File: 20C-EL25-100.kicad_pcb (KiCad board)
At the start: 2 copper layers, 65.5 x 23.5 mm, 9 parts, among them J1 Conn_01x04

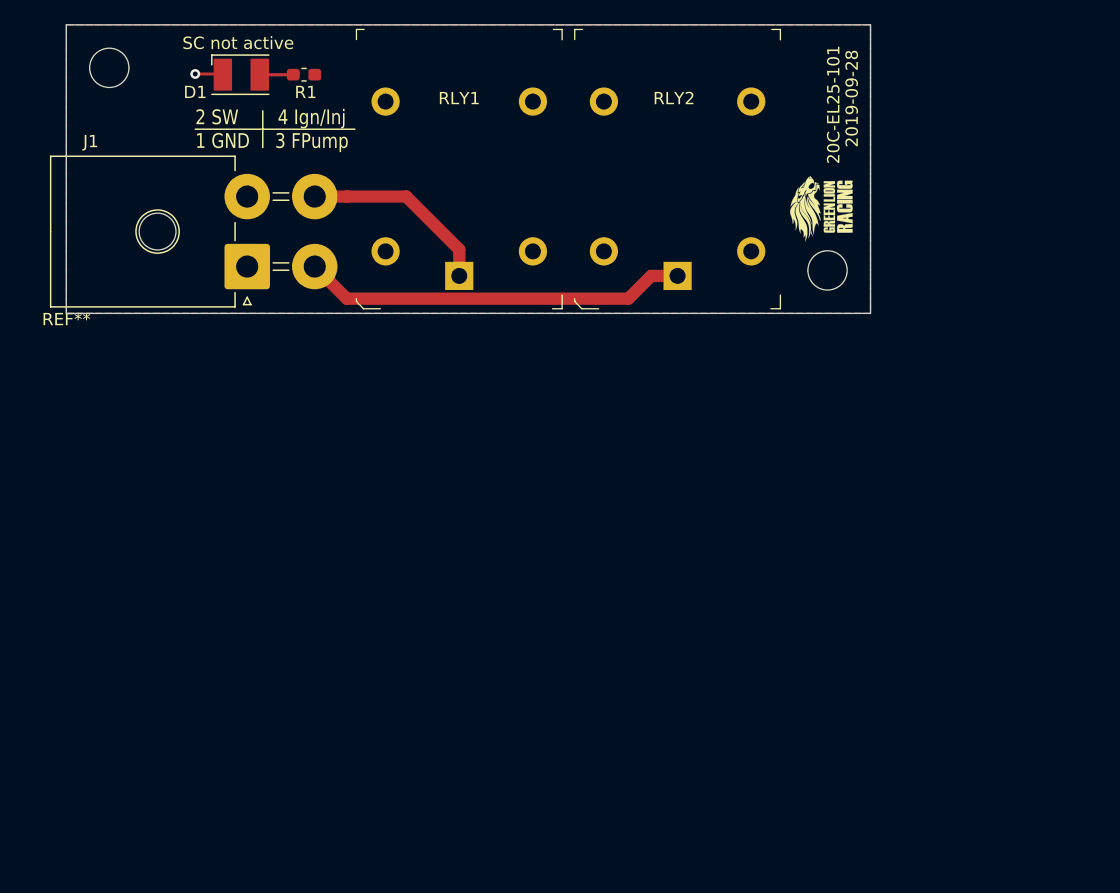
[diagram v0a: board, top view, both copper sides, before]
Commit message: added 3. relays to pcb
added 12V relays on pcb to support our ignition (lowside FET inside MCU)
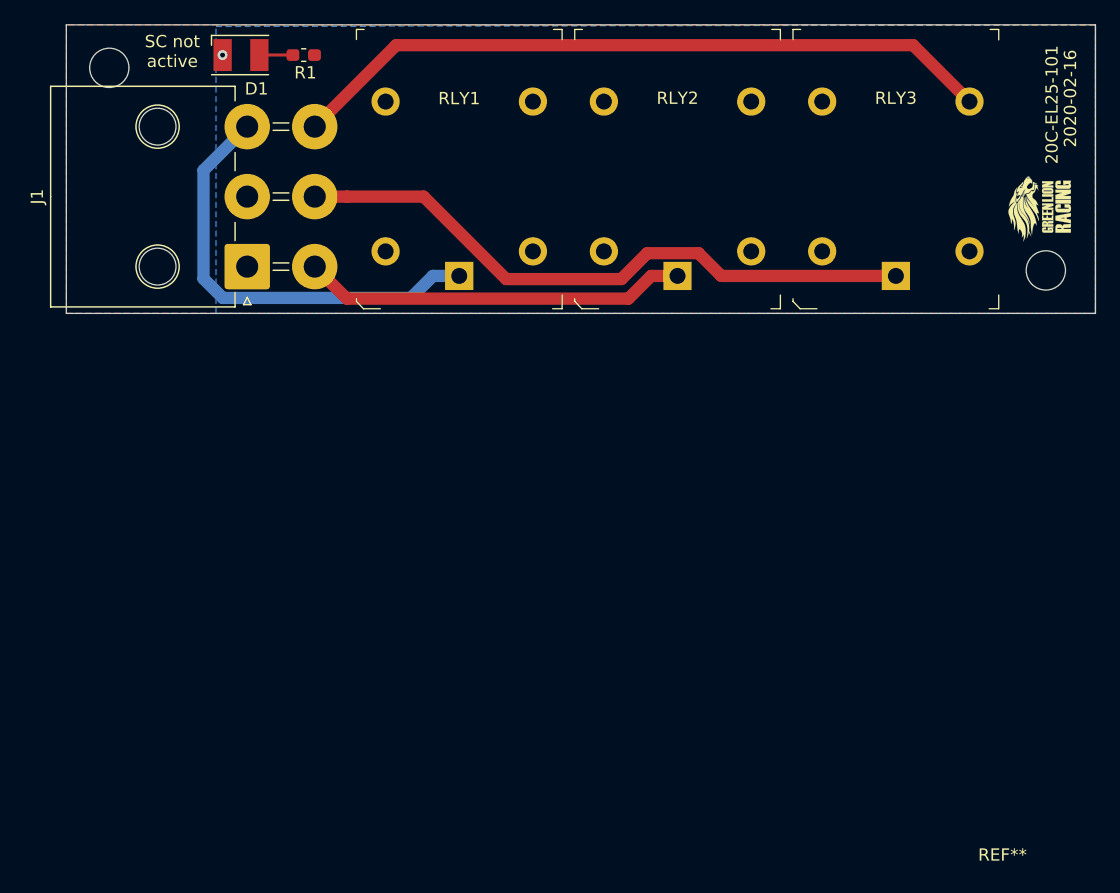
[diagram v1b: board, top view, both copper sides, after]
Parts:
- added RLY3: JSM1-12V-5, digikey-footprints:Relay_JSM1-12V-5, F.Cu at (67.6, -3.05)
- J1: value Conn_01x04 -> Conn_01x06_Female; footprint Connector_Molex:Molex_Mega-Fit_76825-0004_2x02_P5.70mm_Horizontal -> Connector_Molex:Molex_Mega-Fit_76825-0006_2x03_P5.70mm_Horizontal
- moved REF** 87.8 mm to (76.3, 43.6)
- moved G*** 17.8 mm to (79.3, -8.50)
- moved REF** 17.8 mm to (79.8, -3.50)
- moved D1 1.60 mm to (14.2, -21.0)
- moved R1 1.60 mm to (19.3, -21.0)
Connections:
- J1 pad 3: /GND_SW2 -> /GND_SW1
- J1 pad 4: /GND_SW1 -> /GND_SW2
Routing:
- net /12V: track 0.00 -> 58.0 mm
- net /12V_SW1: track 0.00 -> 51.8 mm
- net /GND_SW1: track 15.7 -> 36.1 mm
- net GND: track 2.27 -> 0.00 mm
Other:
- board size 65.5 x 23.5 mm -> 83.8 x 23.5 mm
- board text added: "2020-02-16"
- board text added: "3 FPump 2 SW 1 GND"
- board text added: "6 12V 5 Inj 4 Ign"
- board text removed: "2 SW 1 GND"
- board text removed: "2019-09-28"
- board text removed: "4 Ign/Inj 3 FPump"
